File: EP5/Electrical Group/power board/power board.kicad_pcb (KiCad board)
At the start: 2 copper layers, 96.5 x 61.1 mm, 57 parts, among them IC1 TCR1HF33B,LM_CT, IC2 MCP6C04T-100E_CHY, IC3 MCP6C04T-100E_CHY, IC4 MCP6C04T-100E_CHY, IC5 TCR1HF33B,LM_CT, IC6 MCP6C04T-100E_CHY, IC7 ISO6741DWR, IC8 MCP6C04T-100E_CHY, J1 GLVMS & MP, J3 battery, J4 powertrain, J5 FAN1, J6 FAN2, J7 PWR, J8 PWR_signals, J9 USB_A, U1 MCP3004, U2 MCP3002

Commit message: minor update on power board
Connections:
- net /isolated_interface/CS2 renamed /isolated_interface/CS2_
- net /isolated_interface/CS4 renamed /isolated_interface/CS4-
- IC7 pad 11: /isolated_interface/MISO -> /24V_circuitry/MISO
- IC7 pad 12: /isolated_interface/MOSI -> /24V_circuitry/MOSI
- IC7 pad 14: /isolated_interface/SCK -> /24V_circuitry/SCK
- IC7 pad 3: /isolated_interface/SCK -> /isolated_interface/SCK_
- IC7 pad 5: /isolated_interface/MOSI -> /isolated_interface/MOSI_
- IC7 pad 6: /isolated_interface/MISO -> /isolated_interface/MISO_
- J8 pad 1: /isolated_interface/MOSI -> /isolated_interface/MOSI_
- J8 pad 2: /isolated_interface/MISO -> /isolated_interface/MISO_
- J8 pad 4: /isolated_interface/SCK -> /isolated_interface/SCK_
- U1 pad 10: /isolated_interface/MISO -> /24V_circuitry/MISO
- U1 pad 11: /isolated_interface/SCK -> /24V_circuitry/SCK
- U1 pad 9: /isolated_interface/MOSI -> /24V_circuitry/MOSI
- U2 pad 5: /isolated_interface/MOSI -> /isolated_interface/MOSI_
- U2 pad 6: /isolated_interface/MISO -> /isolated_interface/MISO_
- U2 pad 7: /isolated_interface/SCK -> /isolated_interface/SCK_
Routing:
- net /isolated_interface/SCK: track 62.9 -> 0.00 mm
- net /isolated_interface/SCK_: track 0.00 -> 46.1 mm
- net /isolated_interface/MISO: track 42.3 -> 0.00 mm
- net /isolated_interface/MOSI: track 40.3 -> 0.00 mm
- net /isolated_interface/MISO_: track 0.00 -> 26.2 mm
- net /isolated_interface/MOSI_: track 0.00 -> 26.0 mm
- net /24V_circuitry/SCK: track 0.00 -> 16.8 mm
- net /24V_circuitry/MISO: track 0.00 -> 16.1 mm
- net /24V_circuitry/MOSI: track 0.00 -> 14.3 mm
- net unconnected-(J9-Shield-Pad5): track 0.00 -> 13.1 mm
- net GND: track 13.5 -> 18.5 mm, vias 15 -> 23
- net GNDPWR: track 32.8 -> 34.0 mm, vias 37 -> 39

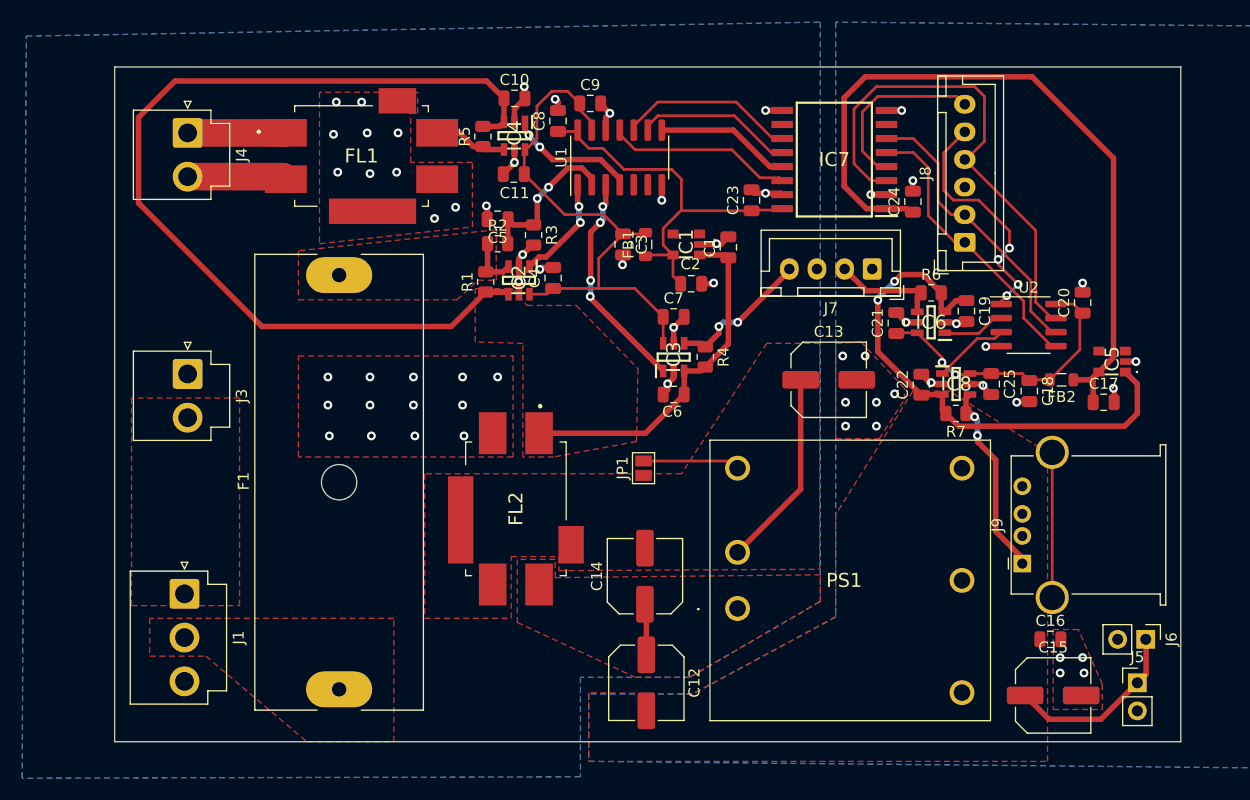
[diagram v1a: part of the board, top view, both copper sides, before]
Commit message: update boards in rear box after Tsou's review
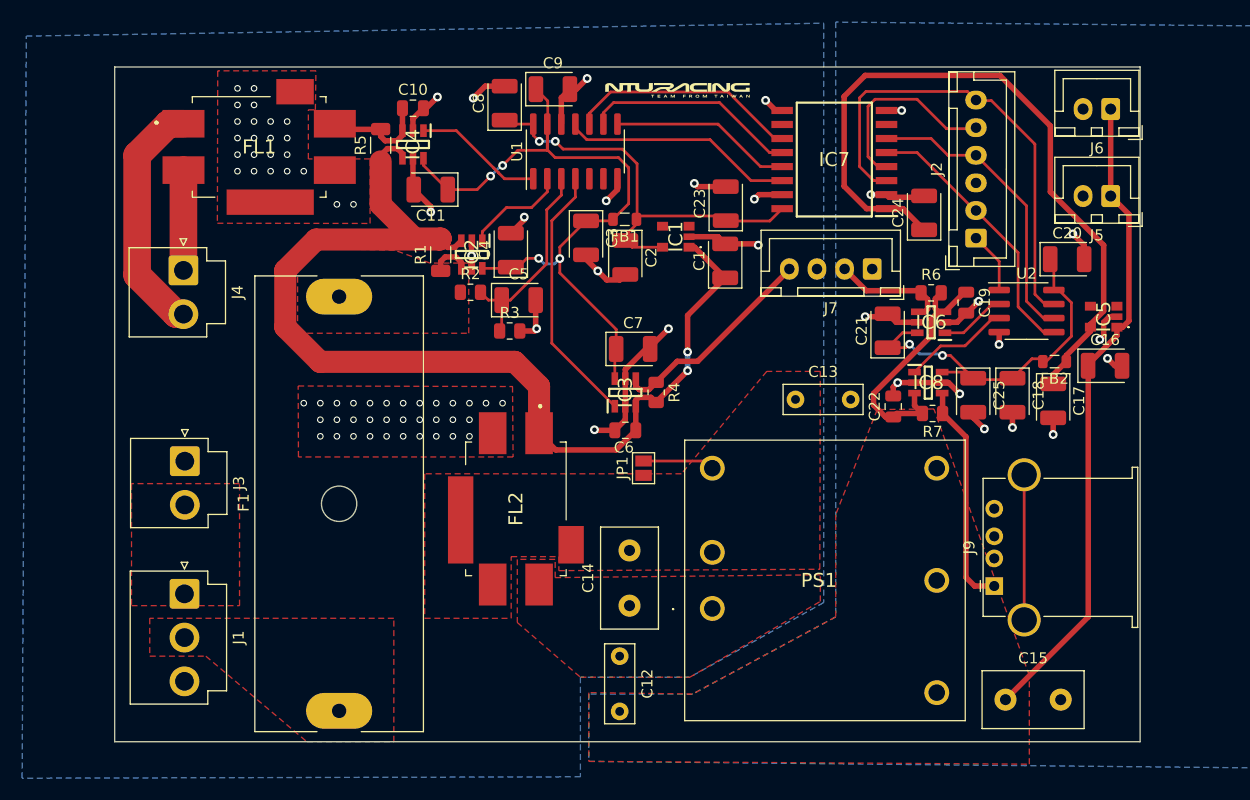
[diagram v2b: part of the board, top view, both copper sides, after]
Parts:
- removed J8: PWR_signals, Connector_JST:JST_XH_B6B-XH-A_1x06_P2.50mm_Vertical
- added J2: PWR_signals, Connector_JST:JST_XH_B6B-XH-A_1x06_P2.50mm_Vertical, F.Cu at (164.6, 52.5)
- C1, C16, C17, C18, C2, C20, C3, C5, C9: footprint Capacitor_SMD:C_0805_2012Metric -> Capacitor_Tantalum_SMD:CP_EIA-3528-15_AVX-H
- C11, C21, C23, C24, C25, C4, C7, C8: value 100n -> 0u1; footprint Capacitor_SMD:C_0805_2012Metric -> Capacitor_Tantalum_SMD:CP_EIA-3528-15_AVX-H
- C12, C13: footprint Capacitor_SMD:C_Elec_6.3x5.8 -> Capacitor_THT:C_Disc_D7.0mm_W2.5mm_P5.00mm
- C14, C15: footprint Capacitor_SMD:C_Elec_6.3x5.8 -> Capacitor_THT:C_Disc_D9.0mm_W5.0mm_P5.00mm
- J5, J6: footprint Connector_PinHeader_2.54mm:PinHeader_1x02_P2.54mm_Vertical -> Connector_JST:JST_XH_B2B-XH-A_1x02_P2.50mm_Vertical
- R1, R5: footprint Resistor_SMD:R_0805_2012Metric -> Resistor_SMD:R_1206_3216Metric
- moved J6 48.1 mm to (176.8, 40.8), turned to 180 degrees
- moved J5 44.1 mm to (176.8, 48.6), turned to 180 degrees
- moved C16 25.3 mm to (176.3, 64.0)
- moved J4 12.5 mm to (92.8, 55.4)
- moved FL1 9.30 mm to (99.7, 44.2)
- moved R5 9.29 mm to (110.7, 44.0)
- moved C10 9.23 mm to (113.6, 40.7)
- moved IC4 9.23 mm to (113.6, 44.0)
- moved R3 8.96 mm to (122.4, 60.9), turned to 0 degrees
- moved J3 7.90 mm to (93.0, 72.6)
- moved C11 7.64 mm to (115.2, 48.1)
- moved C5 7.57 mm to (123.2, 58.1), turned to 0 degrees
- moved C2 6.42 mm to (132.8, 54.2), turned to -90 degrees
- moved R4 5.49 mm to (135.6, 66.4)
- moved C6 5.45 mm to (132.8, 69.8)
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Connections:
- net /24V_circuitry/24V_BAT renamed /24V_circuitry/+24V_BAT
- net /24V_circuitry/24V_profuse renamed /24V_circuitry/+24V_profuse
- net /isolated_interface/24VfiltN renamed /isolated_interface/+24VfiltN
- net /isolated_interface/24VfiltP renamed /isolated_interface/+24VfiltP
- C10 pad 1: +24V -> /24V_circuitry/LV_powertrain
- F1 pad 2: /24V_circuitry/24V_promessure -> /24V_circuitry/+24V_promessure
- IC2 pad 3: /24V_circuitry/24V_promessure -> +24V
- IC2 pad 4: +24V -> /24V_circuitry/+24V_promessure
- IC4 pad 3: +24V -> /24V_circuitry/LV_powertrain
- IC4 pad 4: /24V_circuitry/LV_powertrain -> +24V
- J4 pad 1: Net-(FL1-BIAS) -> Net-(FL1-POWER_SUPPLY_GND)
- J4 pad 2: Net-(FL1-POWER_SUPPLY_GND) -> Net-(FL1-BIAS)
- R1 pad 1: +24V -> /24V_circuitry/+24V_promessure
- R1 pad 2: /24V_circuitry/24V_promessure -> +24V
- R2 pad 1: /24V_circuitry/24V_promessure -> /24V_circuitry/+24V_promessure
- R5 pad 1: /24V_circuitry/LV_powertrain -> +24V
- R5 pad 2: +24V -> /24V_circuitry/LV_powertrain
- U1 pad 1: /24V_circuitry/current_all -> /24V_circuitry/current_powertrain
- U1 pad 2: /24V_circuitry/voltage_all -> /24V_circuitry/current_all
- U1 pad 3: /24V_circuitry/current_rear -> /24V_circuitry/voltage_all
- U1 pad 4: /24V_circuitry/current_powertrain -> /24V_circuitry/current_rear
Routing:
- net GNDPWR: track 34.0 -> 61.9 mm, vias 39 -> 71
- net +24V: track 119.9 -> 99.7 mm, vias 0 -> 2
- net +5V: track 64.8 -> 83.0 mm, vias 2 -> 0
- net /isolated_interface/+24VfiltN: track 18.0 -> 0.00 mm
- net GND: track 18.5 -> 36.1 mm, vias 23 -> 13
- net /isolated_interface/CS2_: track 22.0 -> 5.57 mm, vias 4 -> 0
- net VDDA: track 48.6 -> 62.6 mm, vias 0 -> 4
- net Net-(FL1-BIAS): track 8.89 -> 21.9 mm
- net +3.3VA: track 26.6 -> 34.3 mm
- net /24V_circuitry/LV_rear: track 12.6 -> 19.3 mm, vias 2 -> 0
- net /24V_circuitry/MOSI: track 14.3 -> 19.5 mm
- net /24V_circuitry/MISO: track 16.1 -> 21.0 mm
- net /24V_circuitry/24V_promessure: track 4.87 -> 0.00 mm
- net /isolated_interface/+24VfiltP: track 4.63 -> 0.00 mm
- net /24V_circuitry/voltage_all: track 14.3 -> 18.8 mm, vias 2 -> 0
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- added copper zone on F.Cu, net /24V_circuitry/+24V_promessure
- removed copper zone on F.Cu, net +24V
- removed copper zone on F.Cu, net /24V_circuitry/24V_promessure
- removed copper zone on F.Cu, net GND
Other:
- board size 96.5 x 61.1 mm -> 92.8 x 61.1 mm

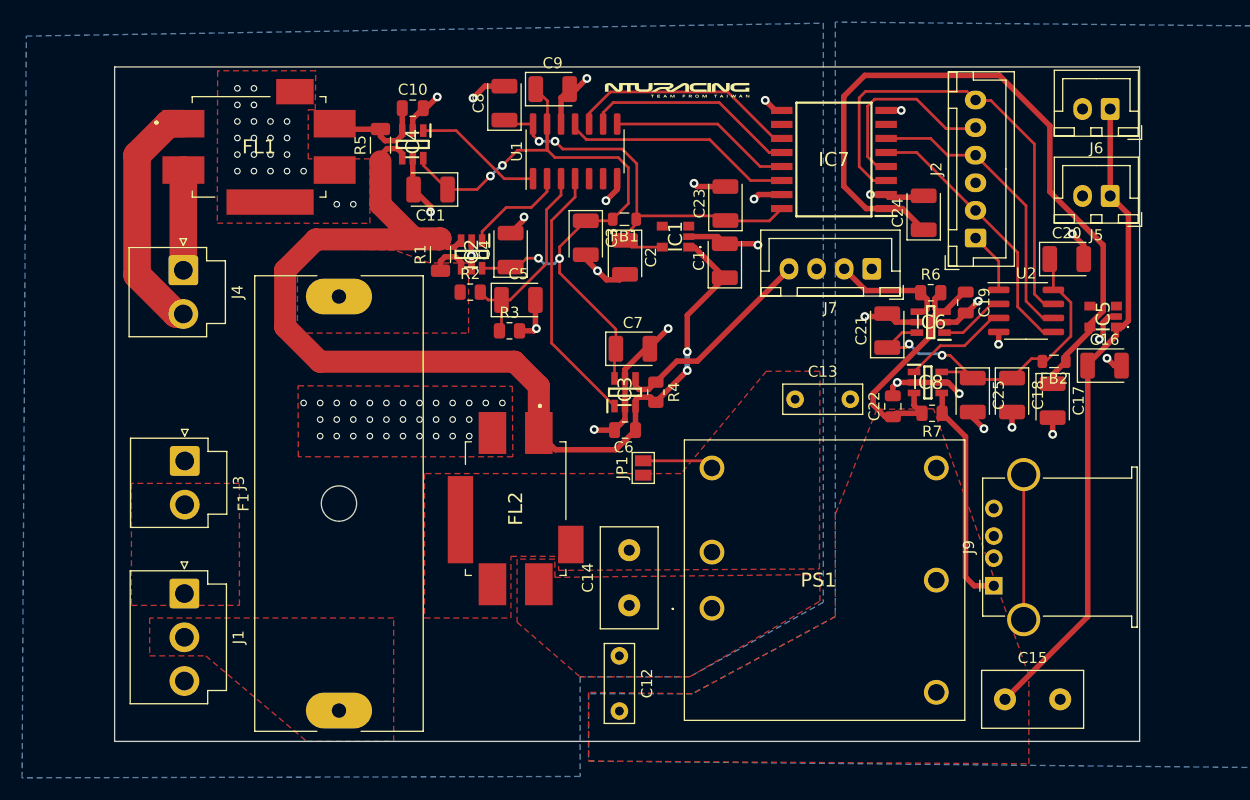
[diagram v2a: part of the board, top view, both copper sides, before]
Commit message: update all boards after Tsou's second review
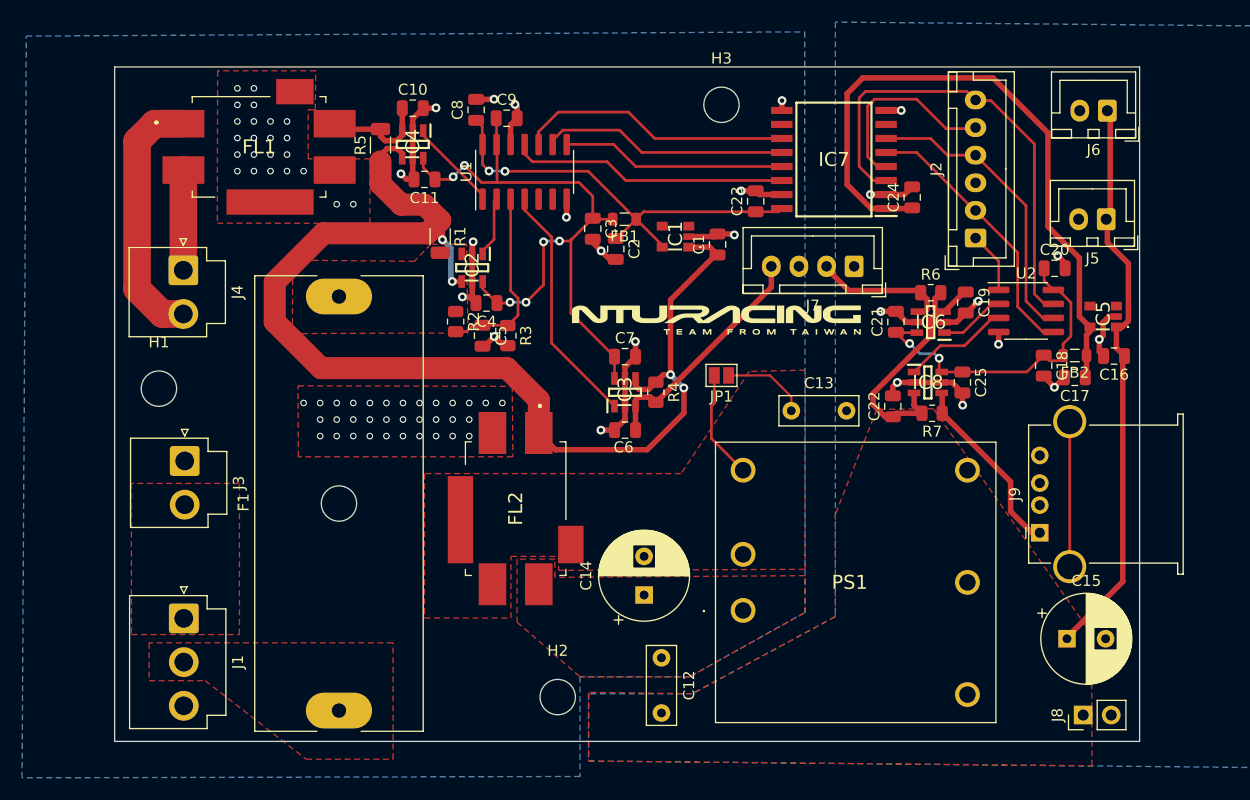
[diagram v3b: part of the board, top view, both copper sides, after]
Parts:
- added H1: MountingHole, MountingHole:MountingHole_3.2mm_M3, F.Cu at (90.6, 66.1)
- added H2: MountingHole, MountingHole:MountingHole_3.2mm_M3, F.Cu at (126.7, 94.0)
- added H3: MountingHole, MountingHole:MountingHole_3.2mm_M3, F.Cu at (141.6, 40.4)
- added J8: 5Vtest, Connector_PinHeader_2.54mm:PinHeader_1x02_P2.54mm_Vertical, F.Cu at (174.3, 95.7)
- C1, C11, C16, C17, C18, C2, C20, C21, C23, C24, C25, C3, C4, C5, C7, C8, C9: footprint Capacitor_Tantalum_SMD:CP_EIA-3528-15_AVX-H -> Capacitor_SMD:C_0805_2012Metric
- C14, C15: footprint Capacitor_THT:C_Disc_D9.0mm_W5.0mm_P5.00mm -> Capacitor_THT:CP_Radial_D8.0mm_P3.50mm
- moved JP1 11.0 mm to (141.6, 64.9), turned to 180 degrees
- moved C15 7.85 mm to (172.9, 88.7)
- moved J9 6.36 mm to (170.4, 79.1)
- moved C4 5.27 mm to (120.3, 58.3), turned to 180 degrees
- moved U1 4.93 mm to (123.7, 46.5)
- moved C9 4.93 mm to (122.1, 41.6)
- moved C5 4.59 mm to (119.9, 61.3), turned to -90 degrees
- moved C18 3.92 mm to (170.8, 64.0)
- moved C12 3.81 mm to (136.1, 90.5)
- moved R2 2.98 mm to (117.5, 60.0), turned to -90 degrees
- moved C17 2.91 mm to (173.6, 65.1), turned to 180 degrees
- moved PS1 2.83 mm to (153.2, 83.6)
- moved C23 2.75 mm to (144.7, 49.1)
- moved C8 2.64 mm to (119.4, 40.8)
- moved J1 2.25 mm to (92.9, 86.9)
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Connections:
- C6 pad 1: +24V -> /24V_circuitry/LV_rear
- IC2 pad 3: +24V -> /24V_circuitry/+24V_promessure
- IC2 pad 4: /24V_circuitry/+24V_promessure -> +24V
- IC3 pad 3: +24V -> /24V_circuitry/LV_rear
- IC3 pad 4: /24V_circuitry/LV_rear -> +24V
- R1 pad 1: /24V_circuitry/+24V_promessure -> +24V
- R1 pad 2: +24V -> /24V_circuitry/+24V_promessure
- R4 pad 1: /24V_circuitry/LV_rear -> +24V
- R4 pad 2: +24V -> /24V_circuitry/LV_rear
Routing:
- net GNDPWR: track 61.9 -> 49.0 mm, vias 71 -> 70
- net +24V: track 99.7 -> 109.3 mm, vias 2 -> 4
- net /isolated_interface/+24VfiltN: track 0.00 -> 7.74 mm
- net +5V: track 83.0 -> 76.0 mm
- net +3.3V: track 65.6 -> 59.8 mm
- net +3.3VA: track 34.3 -> 29.6 mm
- net GND: track 36.1 -> 31.8 mm, vias 13 -> 10
- net /24V_circuitry/current_all: track 9.38 -> 5.16 mm
- net /24V_circuitry/SCK: track 21.1 -> 25.1 mm
- net /24V_circuitry/MISO: track 21.0 -> 24.9 mm
- net /24V_circuitry/CS: track 16.5 -> 20.3 mm
- net /isolated_interface/5V_RPi: track 20.5 -> 16.8 mm
- net /24V_circuitry/+24V_promessure: track 3.63 -> 0.00 mm
- net Net-(JP1-B): track 6.49 -> 9.88 mm
- net /24V_circuitry/current_powertrain: track 11.8 -> 8.43 mm
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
